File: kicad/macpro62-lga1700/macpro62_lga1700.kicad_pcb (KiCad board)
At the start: 10 copper layers, 156 x 167.8 mm, 54 parts, among them J1 J1 CPU-LINK 224 fingers, J3 J3 IOB-HS MCIO RA, J4 J4 SPI TPM, J5 J5 debug UART/SWD, J6 J6 SO-DIMM CH-A (DDR5), J7 J7 SO-DIMM CH-B (DDR5), J8 J8 M.2 2280 boot (PCH x4), Q1 PS C1 SiC654, Q2 PS C2 SiC654, Q3 PS C3 SiC654, Q4 PS C4 SiC654, Q5 PS C5 SiC654, Q6 PS C6 SiC654, Q7 PS GT SiC654, U1 U1 LGA1700 socket PE17007-11N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, U10 U10 BIOS SPI 32MB, U11 eFuse L (VCCCORE VR), U12 eFuse R (rest), U13 U13 i226-V, U14 U14 ALC897 DNP, U2 U2 PCH Z790 FH82Z790, U3 U3 RT3628AE (C3249940), U4 VCCIN_AUX 2ph, U5 VCC1P05/1P8_PROC, U6 PCH rails, U7 5V VIN_BULK, U8 VDD2 1.1V, U9 U9 EC RP2350, Y1 Y1/Y2 38.4M + 32k

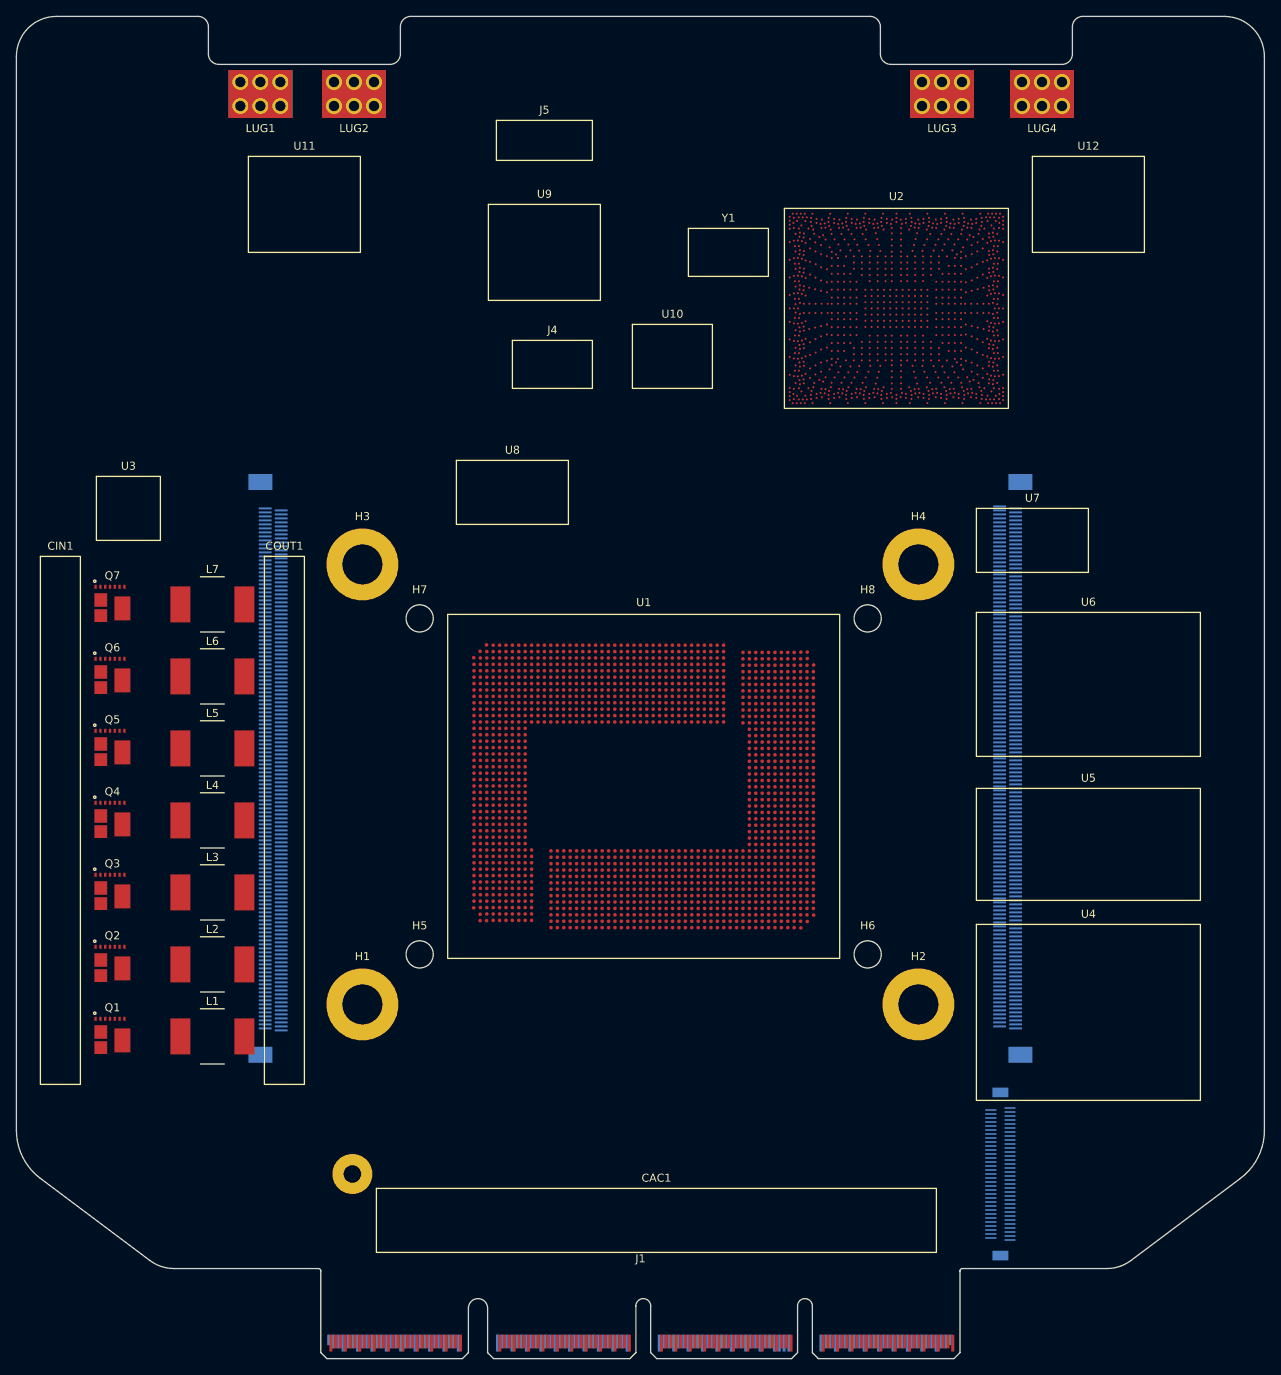
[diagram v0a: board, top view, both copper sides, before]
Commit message: 4x DDR5 DIMM layout for LGA1700 board, traced scans batch 2, spec updates (CR-BP-1, I/O opening map)
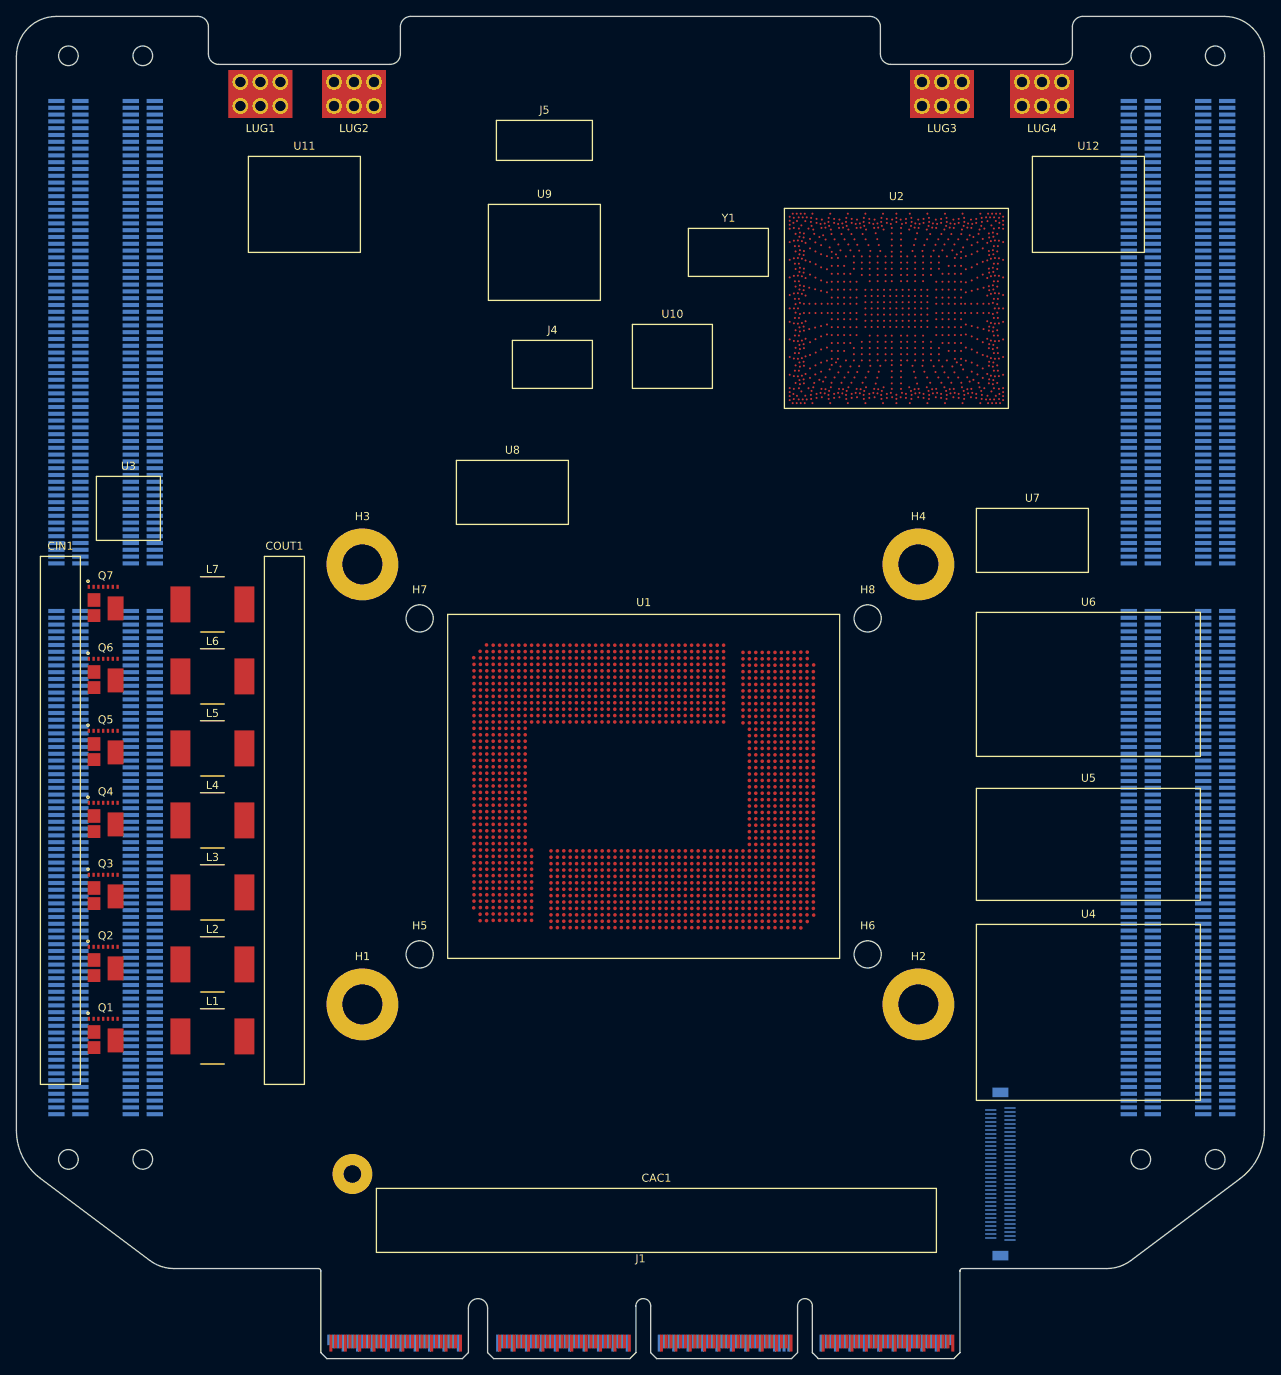
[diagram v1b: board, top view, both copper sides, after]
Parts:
- added J10: J10 CH-B DIMM2 far DDR5 UDIMM, MP62_LGA_Placeholders:MP62_DIMM_DDR5_288P_Vert_UMAX_90414_ShortLatch, B.Cu at (209.8, 144.4)
- added J9: J9 CH-B DIMM1 near DDR5 UDIMM, MP62_LGA_Placeholders:MP62_DIMM_DDR5_288P_Vert_UMAX_90414_ShortLatch, B.Cu at (200.6, 144.4)
- J6: value J6 SO-DIMM CH-A (DDR5) -> J6 CH-A DIMM1 near DDR5 UDIMM; footprint MP62_LGA_Placeholders:MP62_SODIMM_DDR5_262P_RA_UMAX_90415-4015SR -> MP62_LGA_Placeholders:MP62_DIMM_DDR5_288P_Vert_UMAX_90414_ShortLatch
- J7: value J7 SO-DIMM CH-B (DDR5) -> J7 CH-A DIMM2 far DDR5 UDIMM; footprint MP62_LGA_Placeholders:MP62_SODIMM_DDR5_262P_RA_UMAX_90415-4015SR -> MP62_LGA_Placeholders:MP62_DIMM_DDR5_288P_Vert_UMAX_90414_ShortLatch
- U7: value 5V VIN_BULK -> 5V VIN_BULK 4x UDIMM; footprint MP62_LGA_Placeholders:MP62_AREA_5V_SODIMM_VINBULK_14x8 -> MP62_LGA_Placeholders:MP62_AREA_5V_DIMM_VINBULK_14x8
- moved J7 121.7 mm to (66.5, 144.4)
- moved CB1 86.5 mm to (88.0, 185.0)
- moved CB2 86.4 mm to (188.5, 185.0)
- moved J6 24.3 mm to (75.8, 144.4), turned to 90 degrees
- moved Q1 0.85 mm to (71.2, 198.0)
- moved Q2 0.85 mm to (71.2, 189.0)
- moved Q3 0.85 mm to (71.2, 180.0)
- moved Q4 0.85 mm to (71.2, 171.0)
- moved Q5 0.85 mm to (71.2, 162.0)
- moved Q6 0.85 mm to (71.2, 153.0)
- moved Q7 0.85 mm to (71.2, 144.0)
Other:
- board text added: "3 VRM front-left: 6 + 1 phases SiC654 (x 11.15, vias in the back corridor between J7/J6) + Eaton FP4 (5.0 mm); RT3628AE."
- board text added: "5 BACK: 4 x DDR5 UDIMM vertical (UMAX 90414 short latch) at the stock centrelines, 2DPC; M.2 bottom; J3 top; backplate centre."
- board text added: "8 PLACEHOLDERS: real outer dims where sourced (FP4, SiC654, PCH, LGA, M.2, DIMM socket C-90414); pads approximate; no nets."
- board text added: "9 DIMM top <= 33.25 mm off the back (seat 2.0 + 31.25) vs stock DDR3 30.0 + seat: confirm M-CC15; VLP 18.75 UDIMM = fallback."
- board text added: "BACK: 4 x DDR5 UDIMM vertical, module top <= 33.25 off the back (stock DDR3 30.0 + seat) -> confirm M-CC15; CH-A J6 near / J7 far"
- board text added: "CH-B J9 near / J10 far"
- board text added: "DDR0/DDR1 exit the +Y package edge -> left (CH-A J6 near, J7 far) / right (CH-B J9 near, J10 far), daisy chain on L3/L8"
- board text added: "MP62 LGA1700 CPU BOARD (CB) rev A floorplan fl2 - frame: x right, y up from the board bottom, FRONT = socket/core side"
- board text added: "STOCK DDR3 PAIR 22.5-168.2"
- board text added: "VRM via corridor x 9.05-13.25 (between the J7/J6 pad rows)"
- board text removed: "3 VRM front-left: 6 + 1 phases SiC654 + Eaton FP4 (5.0 mm); RT3628AE. Inductor tops 1.3-2.5 mm under the plate -> thermal pads."
- board text removed: "5 BACK: 2 x DDR5 SO-DIMM (UMAX 90415-4015SR, 4 mm) in the stock DIMM strips; M.2 2280 bottom; J3 MCIO RA top; backplate centre."
- board text removed: "8 PLACEHOLDERS: real outer dims where sourced (FP4, SiC654, PCH, LGA, M.2, SO-DIMM module); pads approximate; no nets."
- board text removed: "BACK side strips = stock DIMM zones"
- board text removed: "BACK side strips = stock DIMM zones (proven Z room toward the PSU)"
- board text removed: "DDR0/DDR1 exit the +Y package edge -> fan out left (CH-A J6) and right (CH-B J7) on L3/L8, byte-swizzled"
- board text removed: "MP62 LGA1700 CPU BOARD (CB) rev A floorplan fl1 - frame: x right, y up from the board bottom, FRONT = socket/core side"

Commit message: I/O board rev A0 (6x USB-C DP alt, stock audio/speaker/PSU/button flex) + curved I/O plate v2; CPU board single left 12V entry, GPU bus-bar keep-out
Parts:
- removed LUG3: LUG3 12V?, MP62_LGA_Placeholders:MP62_CB_BusBarLug_8x6_PLACEHOLDER
- removed LUG4: LUG4 GND?, MP62_LGA_Placeholders:MP62_CB_BusBarLug_8x6_PLACEHOLDER
- removed U12: eFuse R (rest), MP62_LGA_Placeholders:MP62_AREA_eFuse_TPS25985_14x12
- U11: value eFuse L (VCCCORE VR) -> U11 eFuse 12V IN (whole CB)
- moved LUG1 2.55 mm to (88.0, 80.2)
- moved LUG2 1.45 mm to (100.8, 80.2)
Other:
- board text added: "-> U11 eFuse -> 12V plane L5+L6 >= 20 mm"
- board text added: "12V SINGLE ENTRY (stock): LUG1/2 top-left"
- board text added: "5b 12V: ONE stock lug pair at the top-left (LUG1 x 27.95, LUG2 x 40.75; photo 2026-10-01) -> one eFuse U11; no right-side lugs."
- board text added: ">= 8 mm across the top band to the right rails"
- board text added: "GPU BUS-BAR PASS-THROUGH (no CB lugs)"
- board text added: "down the left edge to CIN1/VRM (~13 A pk);"
- board text added: "keep-out notch +3 mm, all layers, both sides"
- board text removed: "LUG3 12V?"
- board text removed: "LUG4 GND?"

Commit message: Cross-board compatibility audit: interface control doc, CR-BP-1 applied, J2/J3 row-swap pinouts, 15-pin face AUX, fan header removed from backplane, CPU board i226/BT1 cleanup
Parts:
- removed U13: U13 i226-V, MP62_LGA_Placeholders:MP62_AREA_i226V_10x10
- BT1: value BT1 CR2032 -> BT1 CR2032 DNP (VBAT_RTC from the IOB via J3 B26)
- J3: value J3 IOB-HS MCIO RA -> J3 IOB-HS MCIO 124 RA (host end, docs/mp62-cb-j3_mcio124_host-end.csv)
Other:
- board text added: "DDI lands (bottom-left of the package): DDI-B 4-lane + DDI-C 2-lane DP -> J3 -> IOB C5 / C6 (plan sec. 7, ICD)"
- board text removed: "DDI A-E lands (bottom-left of the package): DDI-1 (native DP) + DDI-2 (USB-C DP-alt) -> J3 IOB (sec. 7 of the plan)"

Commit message: ICD rev 2: 45 deg faces, 445 W ceiling + live power target (INA228 telemetry), ribbon MCIO jog cables, BT on S0, fan fail-safe, port-module I2C map
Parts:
- added U15: U15 INA228 + RS1 0.5 mOhm (12V in, I2C0 0x45), MP62_LGA_Placeholders:MP62_AREA_PwrMon_INA228_10x6, F.Cu at (111.0, 94.0)
